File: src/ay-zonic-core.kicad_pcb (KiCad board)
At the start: 2 copper layers, 61 x 80.6 mm, 31 parts, among them J1 01x10, SW1 SW_DIP_x01, U1 AY-3-8912, U2 74HCT74, U3 74HCT08, U4 74HCT11, U5 74HCT02

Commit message: Signed-off-by: jgratton72 <jon@grattons.co.uk>
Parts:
- U2, U3, U4, U5: footprint Package_DIP:DIP-14_W7.62mm_Socket_LongPads -> Package_DIP:DIP-14_W7.62mm_LongPads
- moved U2 61.4 mm to (75.2, 93.0)
- moved C1 54.3 mm to (122.4, 81.0)
- moved U5 53.5 mm to (122.9, 93.0)
- moved C2 45.9 mm to (116.3, 81.0)
- moved U3 44.6 mm to (89.9, 93.0)
- moved SW1 43.4 mm to (110.7, 92.7), turned to -90 degrees
- moved U1 43.4 mm to (71.4, 56.1), turned to -90 degrees
- moved CO2 40.5 mm to (116.2, 52.2), turned to -90 degrees
- moved U4 39.8 mm to (102.9, 93.0)
- moved RN1 39.1 mm to (68.8, 75.2), turned to 0 degrees
- moved R8 38.7 mm to (114.6, 71.4), turned to 0 degrees
- moved C3 35.5 mm to (122.2, 66.8)
- moved R5 32.6 mm to (108.2, 63.8), turned to 90 degrees
- moved C4 31.8 mm to (117.1, 66.8)
- moved C5 31.2 mm to (68.3, 58.7), turned to 90 degrees
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- renumbered R11 to R8, R10 to R9
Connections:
- J1 pad 1: /IOA0 -> VCC
- J1 pad 2: /IOA1 -> /IOA0
- J1 pad 3: /IOA2 -> /IOA1
- J1 pad 4: /IOA3 -> /IOA2
- J1 pad 5: /IOA4 -> /IOA3
- J1 pad 6: /IOA5 -> /IOA4
- J1 pad 7: /IOA6 -> /IOA5
- J1 pad 8: /IOA7 -> /IOA6
- J1 pad 9: VCC -> /IOA7

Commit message: new back 3D image
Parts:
- SW1: value SW_DIP_x01 -> ZON-X
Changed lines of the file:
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@@
 			)
 		)
-		(property "Value" "SW_DIP_x01"
+		(property "Value" "ZON-X"
 			(at -2.032 0 0)
 			(layer "B.SilkS")

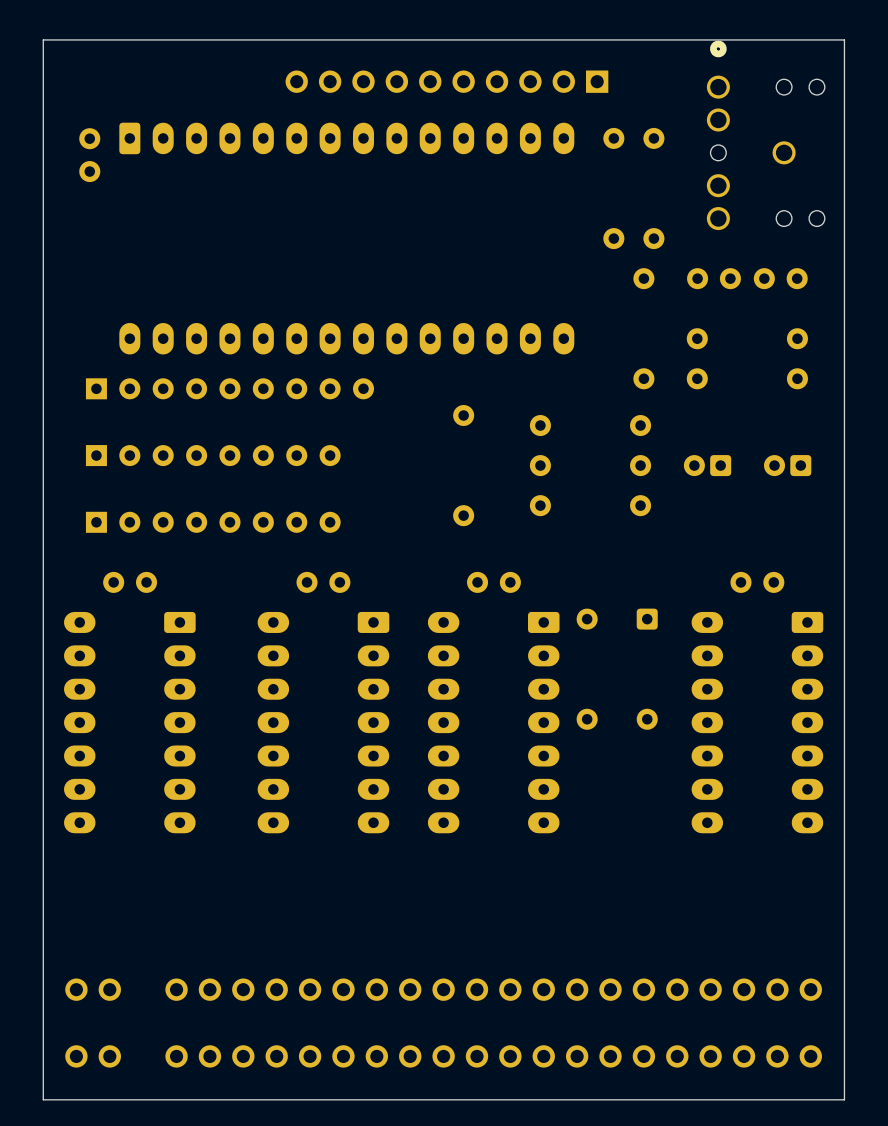
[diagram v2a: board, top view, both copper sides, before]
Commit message: added labels to IO connector
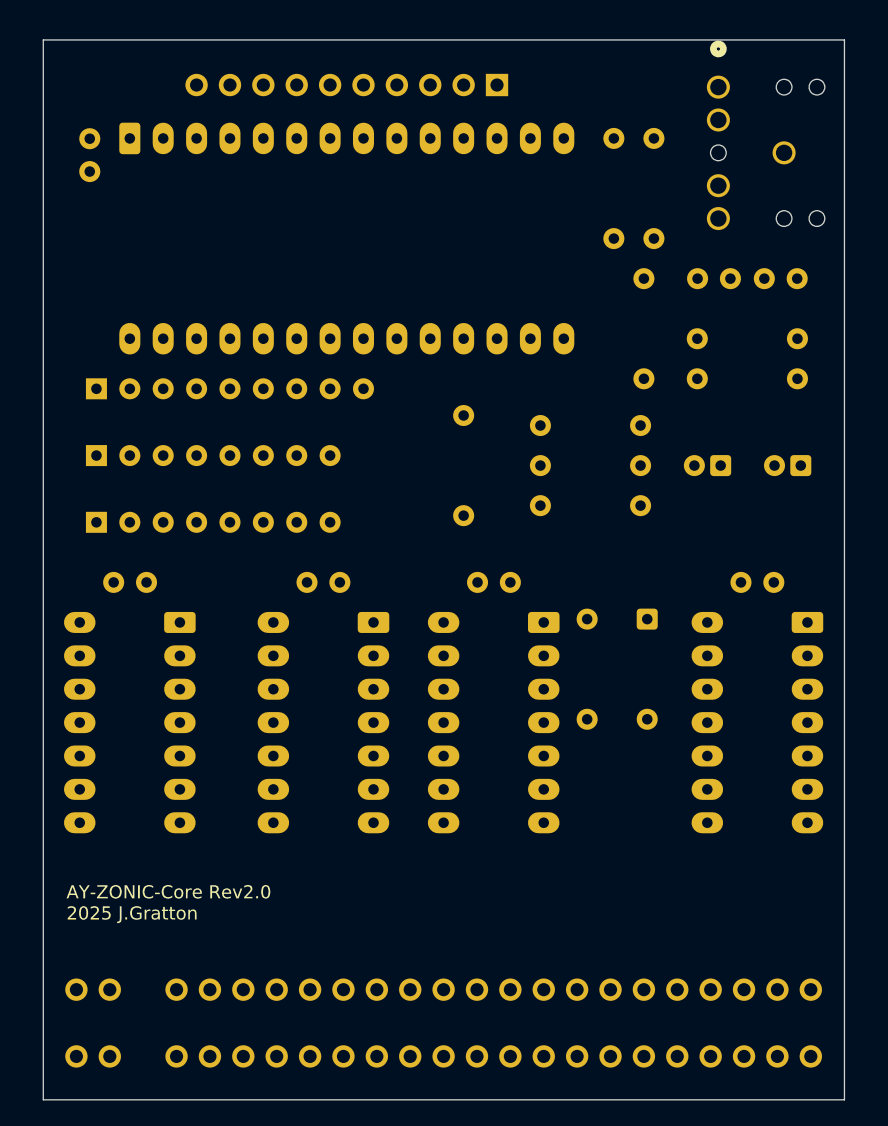
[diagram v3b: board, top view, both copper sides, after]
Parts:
- Line Out: renamed from CO2
- moved I/O 7.62 mm to (99.3, 52.1)
- renumbered J1 to I/O
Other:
- board text added: "AY-ZONIC-Core Rev2.0 2025 J.Gratton"
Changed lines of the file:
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@@
 		(at 116.158 52.23 -90)
 		(tags "SPC21348 ")
-		(property "Reference" "CO2"
-			(at 5 0 90)
+		(property "Reference" "Line Out"
+			(at -2.446 -4.746 180)
 			(unlocked yes)
 			(layer "B.SilkS")
@@
 			(unlocked yes)
 			(layer "B.Fab")
+			(hide yes)
 			(effects
 				(font
@@
 			(layer "B.Fab")
 		)
-		(fp_text user "${REFERENCE}"
-			(at 5 0 90)
-			(unlocked yes)
-			(layer "B.Fab")
-			(effects
-				(font
-					(size 1 1)
-					(thickness 0.15)
-				)
-				(justify mirror)
-			)
-		)
 		(pad "" np_thru_hole circle
 			(at 0 -7.5 270)
@@
 	(footprint "Connector_PinHeader_2.54mm:PinHeader_1x10_P2.54mm_Vertical"
 		(layer "B.Cu")
-		(at 106.934 51.816 90)
+		(at 99.314 52.07 90)
 		(descr "Through hole straight pin header, 1x10, 2.54mm pitch, single row")
 		(tags "Through hole pin header THT 1x10 2.54mm single row")
-		(property "Reference" "J1"
-			(at 0 -25.146 90)
+		(property "Reference" "I/O"
+			(at 0 -25.4 270)
 			(layer "B.SilkS")
 			(effects
@@
 		)
 		(property "Value" "01x10"
-			(at 0 -25.24 90)
+			(at 0 -25.24 270)
 			(layer "B.Fab")
 			(hide yes)
@@
 		)
 		(property "Datasheet" "~"
-			(at 0 0 90)
+			(at 0 0 270)
 			(layer "B.Fab")
 			(hide yes)
@@
 		)
 		(property "Description" "Generic connector, single row, 01x10, script generated"
-			(at 0 0 90)
+			(at 0 0 270)
 			(layer "B.Fab")
 			(hide yes)
@@
 			(layer "B.Fab")
 		)
-		(fp_text user "${REFERENCE}"
-			(at 0 -11.43 0)
-			(layer "B.Fab")
+		(fp_text user "A2"
+			(at 3.048 -7.62 270)
+			(unlocked yes)
+			(layer "B.SilkS")
 			(effects
 				(font
-					(size 1 1)
-					(thickness 0.15)
+					(size 0.6 0.6)
+					(thickness 0.09)
 				)
-				(justify mirror)
+				(justify right mirror)
+			)
+		)
+		(fp_text user "A3"
+			(at 3.048 -10.16 270)
+			(unlocked yes)
+			(layer "B.SilkS")
+			(effects
+				(font
+					(size 0.6 0.6)
+					(thickness 0.09)
+				)
+				(justify right mirror)
+			)
+		)
+		(fp_text user "A4"
+			(at 3.048 -12.7 270)
+			(unlocked yes)
+			(layer "B.SilkS")
+			(effects
+				(font
+					(size 0.6 0.6)
+					(thickness 0.09)
+				)
+				(justify right mirror)
+			)
+		)
+		(fp_text user "A7"
+			(at 3.048 -20.32 270)
+			(unlocked yes)
+			(layer "B.SilkS")
+			(effects
+				(font
+					(size 0.6 0.6)
+					(thickness 0.09)
+				)
+				(justify right mirror)
+			)
+		)
+		(fp_text user "-"
+			(at 2.54 -22.86 270)
+			(unlocked yes)
+			(layer "B.SilkS")
+			(effects
+				(font
+					(size 0.6 0.6)
+					(thickness 0.09)
+				)
+				(justify right mirror)
+			)
+		)
+		(fp_text user "5v"
+			(at 3.048 0 270)
+			(unlocked yes)
+			(layer "B.SilkS")
+			(effects
+				(font
+					(size 0.6 0.6)
+					(thickness 0.09)
+				)
+				(justify right mirror)
+			)
+		)
+		(fp_text user "A6"
+			(at 3.048 -17.78 270)
+			(unlocked yes)
+			(layer "B.SilkS")
+			(effects
+				(font
+					(size 0.6 0.6)
+					(thickness 0.09)
+				)
+				(justify right mirror)
+			)
+		)
+		(fp_text user "A5"
+			(at 3.048 -15.24 270)
+			(unlocked yes)
+			(layer "B.SilkS")
+			(effects
+				(font
+					(size 0.6 0.6)
+					(thickness 0.09)
+				)
+				(justify right mirror)
+			)
+		)
+		(fp_text user "A1"
+			(at 3.048 -5.08 270)
+			(unlocked yes)
+			(layer "B.SilkS")
+			(effects
+				(font
+					(size 0.6 0.6)
+					(thickness 0.09)
+				)
+				(justify right mirror)
+			)
+		)
+		(fp_text user "A0"
+			(at 3.048 -2.54 270)
+			(unlocked yes)
+			(layer "B.SilkS")
+			(effects
+				(font
+					(size 0.6 0.6)
+					(thickness 0.09)
+				)
+				(justify right mirror)
 			)
 		)
@@
 		(layer "Edge.Cuts")
 	)
+	(gr_text "AY-ZONIC-Core Rev2.0\n2025 J.Gratton"
+		(at 66.548 114.3 0)
+		(layer "F.SilkS")
+		(effects
+			(font
+				(size 1 1)
+				(thickness 0.1)
+			)
+			(justify left)
+		)
+	)
 	(embedded_fonts no)

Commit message: routed and new images
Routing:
- net VCC: track 0.00 -> 234.9 mm, vias 0 -> 1
- net GND: track 0.00 -> 224.3 mm
- net /PSGCLK: track 0.00 -> 69.2 mm, vias 0 -> 2
- net /~{RESET}: track 0.00 -> 56.9 mm
- net /D4: track 0.00 -> 55.6 mm, vias 0 -> 1
- net Net-(U3-Pad11): track 0.00 -> 51.7 mm, vias 0 -> 2
- net /D2: track 0.00 -> 47.6 mm
- net /BC1: track 0.00 -> 47.2 mm, vias 0 -> 1
- net /D7: track 0.00 -> 46.5 mm, vias 0 -> 1
- net GND_AUDIO: track 0.00 -> 46.0 mm
- net /D0: track 0.00 -> 45.2 mm, vias 0 -> 1
- net /OUTA: track 0.00 -> 44.0 mm
- net /D1: track 0.00 -> 42.5 mm
- net /D3: track 0.00 -> 42.1 mm
- net /A0: track 0.00 -> 41.3 mm, vias 0 -> 1
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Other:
- board size 61 x 80.6 mm -> 63.5 x 80.1 mm
